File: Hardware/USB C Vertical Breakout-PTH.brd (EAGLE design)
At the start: 11.4 x 20.3 mm, 31 parts

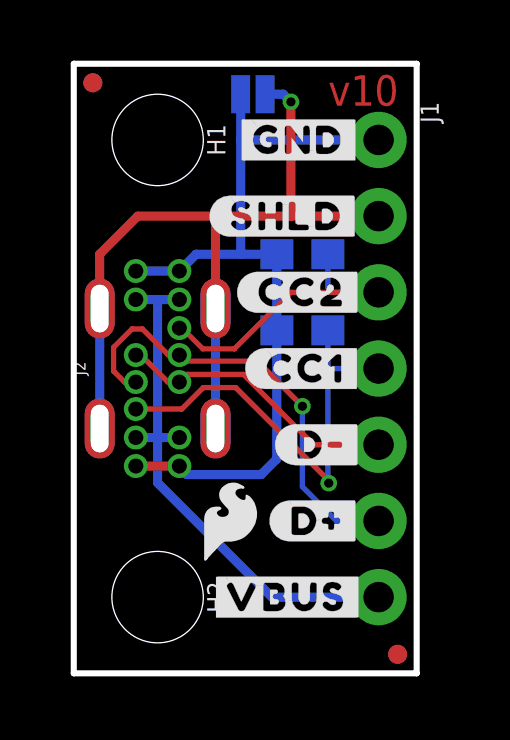
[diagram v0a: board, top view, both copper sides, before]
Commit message: Repo Restructure, Work to board
Finished the new connector and the board layout; updates to schematic
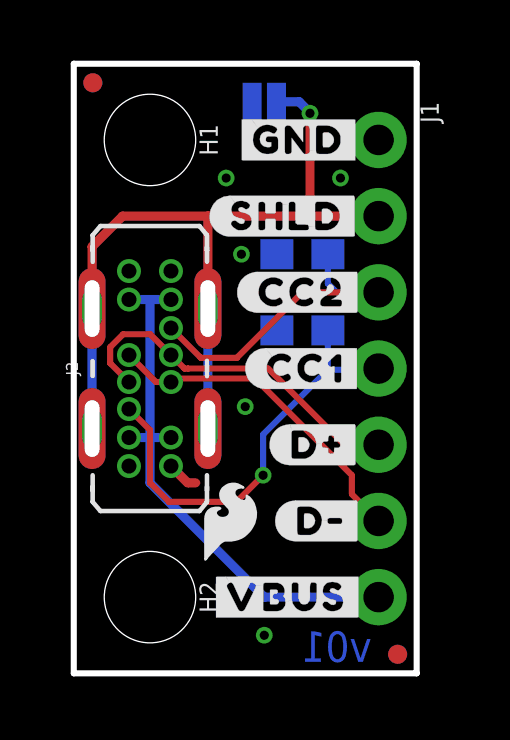
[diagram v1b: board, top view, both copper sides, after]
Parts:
- J2: device USB C Vertical:USB-C-8P-2LAYER-VERTICAL-PTH -> USB-C_Vertical:USB-C-8P-2LAYER-VERTICAL-PTH
- moved FRAME2 25.7 mm to (-20.3, -35.6)
- moved U$12 2.54 mm to (8.26, 5.08)
- moved U$6 2.54 mm to (8.26, 7.62)
- moved U$7 2.54 mm to (8.13, 7.62)
- moved U$8 2.54 mm to (8.26, 5.08)
- moved SHLD 0.46 mm to (6.35, 19.1)
- moved H1 0.25 mm to (2.54, 17.8)
- moved H2 0.25 mm to (2.54, 2.54)
- moved J2 0.25 mm to (2.54, 10.2)
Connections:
- net D+: now also J1.5; no longer J1.6
- net D-: now also J1.6; no longer J1.5
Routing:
- net GND: track 26.8 -> 1.06 mm, vias 0 -> 5
- net D+: track 15.0 -> 12.1 mm, vias 1 -> 0
- net D-: track 9.54 -> 11.1 mm
- added copper zone on layer 1, net GND
- added copper zone on layer 16, net GND
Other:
- board text added: "v01"
- board text removed: "v10"

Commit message: PCB files ready for order
Made updates to schematic and layout as per the design review - see design review document for more detailed information. Added gerber files and BOM files for PCB assembly at JLC.
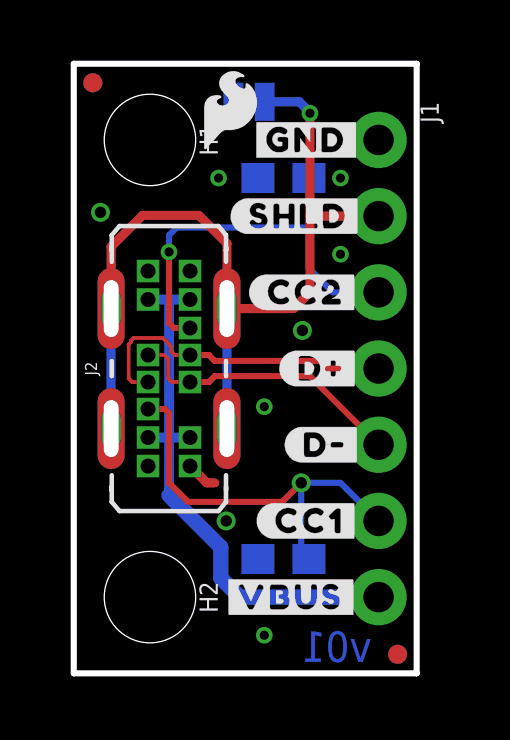
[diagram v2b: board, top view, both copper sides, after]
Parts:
- removed U$11, U$2: (no value), output:#VBUS#0
- removed U$12: (no value), output:#_D##2
- removed U$13: (no value), output:#_SHLD#0
- removed U$14: (no value), output:#CC1#0
- removed U$15: (no value), output:#_CC2#1
- removed U$3, U$9: (no value), output:#GND#5
- removed U$5: (no value), output:#_CC1#0
- removed U$6: (no value), output:#_D##1
- removed U$8: (no value), output:#D##2
- added U$16: (no value), output:#CC2#0
- added U$17: (no value), output:#CC1#5
- added U$18: (no value), output:#SHLD#5
- added U$19, U$20: (no value), output:#VBUS#7
- added U$21: (no value), output:#GND#6
- added U$22: (no value), output:#SHLD#8
- added U$23: (no value), output:#CC2#9
- added U$24: (no value), output:#D##9
- added U$25: (no value), output:#D##10
- added U$26: (no value), output:#CC1#11
- SHLD: device SparkFun-Jumpers:SMT-JUMPER_2_NO_NO-SILK -> SparkFun-Jumpers:SMT-JUMPER_2_NC_TRACE_NO-SILK
- U$10: device output:#SHLD#1 -> output:#GND#6
- U$4: device output:#CC2#1 -> output:#D##3
- U$7: device output:#D##1 -> output:#D##4
- moved LOGO3 13.7 mm to (5.21, 18.8)
- moved R1 7.65 mm to (6.99, 3.81)
- moved LOGO2 3.18 mm to (1.65, 5.33)
- moved R2 2.62 mm to (6.99, 16.5)
- moved U$10 2.62 mm to (7.75, 17.8)
- moved U$4 2.62 mm to (8.26, 10.2)
- moved U$1 0.90 mm to (8.38, 19.3)
- moved J2 0.63 mm to (3.17, 10.2)
- moved SHLD 0.51 mm to (5.84, 19.1)
- moved U$7 0.25 mm to (8.38, 7.62)
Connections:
- net CC1: now also J1.6; no longer J1.4
- net D+: now also J1.4; no longer J1.5
- net D-: now also J1.5; no longer J1.6
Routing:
- net CC2: track 11.0 -> 14.1 mm, vias 0 -> 1
- net SHLD: track 27.8 -> 29.8 mm
- net D-: track 11.1 -> 9.46 mm
- net D+: track 12.1 -> 10.8 mm
- net CC1: track 14.6 -> 13.8 mm
- net GND: vias 5 -> 8
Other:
- board text added: "Solder Mask: Red Thickness: 1.6mm Two layer design Finish: HASL Lead-Free Copper Weight: 1oz Material: TG135-140"
- board text removed: "Solder Mask: Red Thickness: 1.6mm Two layer design Finish: HASL Lead-Free"
